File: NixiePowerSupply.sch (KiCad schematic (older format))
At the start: 1 part

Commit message: Preliminary schematic capture
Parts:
- added C1: 100uF, 35V, symbol CP
- added C2, C3: 100n, symbol C
- added C4: 4u7,250V, symbol CP
- added C5: 10uF,25V, symbol CP
- added D1: ES2F, symbol D
- added J?: BARREL_JACK, symbol BARREL_JACK
- added L1: 100uH, symbol L
- added R1: 10K, symbol R
- added R2: 1M5, symbol R
- added R?: RTRIM, symbol RTRIM
- added Rsense: 50m, symbol R
- added T1: IRF644, symbol IRF644
- gave numbers to parts that had none: 1
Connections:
- net labels added: GND, VCC
- wire segments 0 -> 38

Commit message: Add output capcacitor
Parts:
- added C6: 100nF, 250V, symbol C
- gave numbers to parts that had none: 1
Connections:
- wire segments 38 -> 42
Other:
- moved on the sheet: C4, D1, R1, R2, Rsense, T1
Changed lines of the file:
@@
 L IRF644 T1
 U 1 1 58D729C3
-P 6800 3400
-F 0 "T1" H 7000 3475 50  0000 L CNN
-F 1 "IRF644" H 7000 3400 50  0000 L CNN
-F 2 "" H 7000 3300 50  0001 L CIN
-F 3 "" H 6800 3400 50  0001 L CNN
-	1    6800 3400
+P 6600 3400
+F 0 "T1" H 6800 3475 50  0000 L CNN
+F 1 "IRF644" H 6800 3400 50  0000 L CNN
+F 2 "" H 6800 3300 50  0001 L CIN
+F 3 "" H 6600 3400 50  0001 L CNN
+	1    6600 3400
 	1    0    0    -1
 $EndComp
@@
 Connection ~ 4650 2600
 Wire Wire Line
-	6000 2600 6900 2600
-Wire Wire Line
-	6900 2600 6900 3200
-Wire Wire Line
-	6250 3450 6600 3450
+	6700 2600 6700 3200
 $Comp
 L CP C5
@@
 	5750 4300 5750 4000
 Wire Wire Line
-	3900 4300 8100 4300
+	8300 4300 3900 4300
 $Comp
 L GND #PWR?
@@
 L R Rsense
 U 1 1 58D73575
-P 6900 4050
-F 0 "Rsense" V 6980 4050 50  0000 C CNN
-F 1 "50m" V 6900 4050 50  0000 C CNN
-F 2 "" V 6830 4050 50  0001 C CNN
-F 3 "" H 6900 4050 50  0001 C CNN
-	1    6900 4050
-	1    0    0    -1
-$EndComp
-Wire Wire Line
-	6900 4300 6900 4200
+P 6700 4050
+F 0 "Rsense" V 6780 4050 50  0000 C CNN
+F 1 "50m" V 6700 4050 50  0000 C CNN
+F 2 "" V 6630 4050 50  0001 C CNN
+F 3 "" H 6700 4050 50  0001 C CNN
+	1    6700 4050
+	1    0    0    -1
+$EndComp
+Wire Wire Line
+	6700 4300 6700 4200
 Connection ~ 5750 4300
 Wire Wire Line
-	6900 3600 6900 3900
-Wire Wire Line
-	6750 3600 6750 3650
-Wire Wire Line
-	6750 3650 6900 3650
-Connection ~ 6900 3650
-Wire Wire Line
-	6750 3600 6250 3600
+	6700 3600 6700 3900
+Wire Wire Line
+	6550 3600 6550 3650
+Wire Wire Line
+	6550 3650 6700 3650
+Connection ~ 6700 3650
 $Comp
 L D D1
 U 1 1 58D73EA6
-P 7250 3050
-F 0 "D1" H 7250 3150 50  0000 C CNN
-F 1 "ES2F" H 7250 2950 50  0000 C CNN
-F 2 "" H 7250 3050 50  0001 C CNN
-F 3 "" H 7250 3050 50  0001 C CNN
-	1    7250 3050
+P 7050 3050
+F 0 "D1" H 7050 3150 50  0000 C CNN
+F 1 "ES2F" H 7050 2950 50  0000 C CNN
+F 2 "" H 7050 3050 50  0001 C CNN
+F 3 "" H 7050 3050 50  0001 C CNN
+	1    7050 3050
 	-1   0    0    1
 $EndComp
@@
 L CP C4
 U 1 1 58D74125
-P 7650 3400
-F 0 "C4" H 7675 3500 50  0000 L CNN
-F 1 "4u7,250V" H 7250 3300 50  0000 L CNN
-F 2 "" H 7688 3250 50  0001 C CNN
-F 3 "" H 7650 3400 50  0001 C CNN
-	1    7650 3400
-	1    0    0    -1
-$EndComp
-Wire Wire Line
-	7100 3050 6900 3050
-Connection ~ 6900 3050
-Wire Wire Line
-	7400 3050 8100 3050
-Wire Wire Line
-	7650 3050 7650 3250
-Wire Wire Line
-	7650 4300 7650 3550
-Connection ~ 6900 4300
+P 7350 3500
+F 0 "C4" H 7375 3600 50  0000 L CNN
+F 1 "4u7,250V" H 6950 3400 50  0000 L CNN
+F 2 "" H 7388 3350 50  0001 C CNN
+F 3 "" H 7350 3500 50  0001 C CNN
+	1    7350 3500
+	1    0    0    -1
+$EndComp
+Wire Wire Line
+	6900 3050 6700 3050
+Connection ~ 6700 3050
+Wire Wire Line
+	7200 3050 8300 3050
+Wire Wire Line
+	7350 3050 7350 3350
+Wire Wire Line
+	7350 4300 7350 3650
+Connection ~ 6700 4300
 $Comp
 L R R2
 U 1 1 58D74231
-P 8100 3250
-F 0 "R2" V 8180 3250 50  0000 C CNN
-F 1 "1M5" V 8100 3250 50  0000 C CNN
-F 2 "" V 8030 3250 50  0001 C CNN
-F 3 "" H 8100 3250 50  0001 C CNN
-	1    8100 3250
+P 7900 3250
+F 0 "R2" V 7980 3250 50  0000 C CNN
+F 1 "1M5" V 7900 3250 50  0000 C CNN
+F 2 "" V 7830 3250 50  0001 C CNN
+F 3 "" H 7900 3250 50  0001 C CNN
+	1    7900 3250
 	1    0    0    -1
 $EndComp
@@
 L R R1
 U 1 1 58D74274
-P 8100 4100
-F 0 "R1" V 8180 4100 50  0000 C CNN
-F 1 "10K" V 8100 4100 50  0000 C CNN
-F 2 "" V 8030 4100 50  0001 C CNN
-F 3 "" H 8100 4100 50  0001 C CNN
-	1    8100 4100
-	1    0    0    -1
-$EndComp
-Wire Wire Line
-	8100 3900 8100 3950
-$Comp
-L RTRIM R?
+P 7900 4100
+F 0 "R1" V 7980 4100 50  0000 C CNN
+F 1 "10K" V 7900 4100 50  0000 C CNN
+F 2 "" V 7830 4100 50  0001 C CNN
+F 3 "" H 7900 4100 50  0001 C CNN
+	1    7900 4100
+	1    0    0    -1
+$EndComp
+Wire Wire Line
+	7900 3900 7900 3950
+$Comp
+L RTRIM VR1
 U 1 1 58D74396
-P 8100 3750
-F 0 "R?" V 8200 3650 50  0000 L CNN
-F 1 "RTRIM" V 8000 3725 50  0000 L CNN
-F 2 "" V 8030 3750 50  0001 C CNN
-F 3 "" H 8100 3750 50  0001 C CNN
-	1    8100 3750
-	1    0    0    -1
-$EndComp
-Wire Wire Line
-	8100 3050 8100 3100
-Connection ~ 7650 3050
-Wire Wire Line
-	8100 3400 8100 3600
-Wire Wire Line
-	8100 4300 8100 4250
-Connection ~ 7650 4300
-Wire Wire Line
-	6250 3750 7900 3750
-Wire Wire Line
-	7900 3750 7900 3500
-Wire Wire Line
-	7900 3500 8100 3500
-Connection ~ 8100 3500
+P 7900 3750
+F 0 "VR1" V 8000 3650 50  0000 L CNN
+F 1 "RTRIM" V 7800 3725 50  0000 L CNN
+F 2 "" V 7830 3750 50  0001 C CNN
+F 3 "" H 7900 3750 50  0001 C CNN
+	1    7900 3750
+	1    0    0    -1
+$EndComp
+Wire Wire Line
+	7900 3050 7900 3100
+Connection ~ 7350 3050
+Wire Wire Line
+	7900 3400 7900 3600
+Wire Wire Line
+	7900 4300 7900 4250
+Connection ~ 7350 4300
+Wire Wire Line
+	7700 3750 7700 3500
+Wire Wire Line
+	7700 3500 7900 3500
+Connection ~ 7900 3500
+$Comp
+L C C6
+U 1 1 58D7E2B2
+P 8300 3650
+F 0 "C6" H 8325 3750 50  0000 L CNN
+F 1 "100nF, 250V" H 8325 3550 50  0000 L CNN
+F 2 "" H 8338 3500 50  0000 C CNN
+F 3 "" H 8300 3650 50  0000 C CNN
+	1    8300 3650
+	1    0    0    -1
+$EndComp
+Wire Wire Line
+	6000 2600 6700 2600
+Wire Wire Line
+	6250 3450 6400 3450
+Wire Wire Line
+	6250 3600 6550 3600
+Wire Wire Line
+	6250 3750 7700 3750
+Wire Wire Line
+	8300 3050 8300 3500
+Connection ~ 7900 3050
+Wire Wire Line
+	8300 3800 8300 4300
+Connection ~ 7900 4300
+Wire Wire Line
+	8300 3300 8500 3300
+Connection ~ 8300 3300
+Wire Wire Line
+	8300 4050 8500 4050
+Connection ~ 8300 4050
 $EndSCHEMATC

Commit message: Assigned some footprints.
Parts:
- C1, C5: footprint (none) -> Capacitors_Tantalum_SMD:CP_Tantalum_Case-X_EIA-7343-43_Hand
- C2, C3: footprint (none) -> Capacitors_SMD:C_0805_HandSoldering
- R1: footprint (none) -> Resistors_SMD:R_0805_HandSoldering
- R2: footprint (none) -> Resistors_SMD:R_2512_HandSoldering
- Rsense1: renamed from Rsense; footprint (none) -> Resistors_SMD:R_2010_HandSoldering
- T1: footprint (none) -> TO_SOT_Packages_THT:TO-220_Vertical
- U1: footprint (none) -> Housings_SOIC:SOIC-8_3.9x4.9mm_Pitch1.27mm
- gave numbers to parts that had none: 1
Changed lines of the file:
@@
 F 0 "U1" H 5850 2850 60  0000 C CNN
 F 1 "MAX1771" H 6000 3400 60  0000 C CNN
-F 2 "" H 5750 3350 60  0001 C CNN
+F 2 "Housings_SOIC:SOIC-8_3.9x4.9mm_Pitch1.27mm" H 5750 3350 60  0001 C CNN
 F 3 "" H 5750 3350 60  0001 C CNN
 	1    5750 3350
@@
 F 0 "C1" H 4675 2850 50  0000 L CNN
 F 1 "100uF, 35V" H 4675 2650 50  0000 L CNN
-F 2 "" H 4688 2600 50  0001 C CNN
+F 2 "Capacitors_Tantalum_SMD:CP_Tantalum_Case-X_EIA-7343-43_Hand" H 4688 2600 50  0001 C CNN
 F 3 "" H 4650 2750 50  0001 C CNN
 	1    4650 2750
@@
 F 0 "T1" H 6800 3475 50  0000 L CNN
 F 1 "IRF644" H 6800 3400 50  0000 L CNN
-F 2 "" H 6800 3300 50  0001 L CIN
+F 2 "TO_SOT_Packages_THT:TO-220_Vertical" H 6800 3300 50  0001 L CIN
 F 3 "" H 6600 3400 50  0001 L CNN
 	1    6600 3400
@@
 $EndComp
 $Comp
-L GND #PWR?
+L GND #PWR01
 U 1 1 58D72A4A
 P 4650 2950
-F 0 "#PWR?" H 4650 2700 50  0001 C CNN
+F 0 "#PWR01" H 4650 2700 50  0001 C CNN
 F 1 "GND" H 4650 2800 50  0000 C CNN
 F 2 "" H 4650 2950 50  0001 C CNN
@@
 F 0 "C5" H 4325 3950 50  0000 L CNN
 F 1 "10uF,25V" H 3950 3750 50  0000 L CNN
-F 2 "" H 4338 3700 50  0001 C CNN
+F 2 "Capacitors_Tantalum_SMD:CP_Tantalum_Case-X_EIA-7343-43_Hand" H 4338 3700 50  0001 C CNN
 F 3 "" H 4300 3850 50  0001 C CNN
 	1    4300 3850
@@
 	4650 2900 4650 2950
 $Comp
-L VCC #PWR?
+L VCC #PWR02
 U 1 1 58D72D8A
 P 4100 2550
-F 0 "#PWR?" H 4100 2400 50  0001 C CNN
+F 0 "#PWR02" H 4100 2400 50  0001 C CNN
 F 1 "VCC" H 4100 2700 50  0000 C CNN
 F 2 "" H 4100 2550 50  0001 C CNN
@@
 F 0 "C2" H 4675 3950 50  0000 L CNN
 F 1 "100n" H 4450 3750 50  0000 L CNN
-F 2 "" H 4688 3700 50  0001 C CNN
+F 2 "Capacitors_SMD:C_0805_HandSoldering" H 4688 3700 50  0001 C CNN
 F 3 "" H 4650 3850 50  0001 C CNN
 	1    4650 3850
@@
 F 0 "C3" H 4975 3950 50  0000 L CNN
 F 1 "100n" H 4750 3750 50  0000 L CNN
-F 2 "" H 4988 3700 50  0001 C CNN
+F 2 "Capacitors_SMD:C_0805_HandSoldering" H 4988 3700 50  0001 C CNN
 F 3 "" H 4950 3850 50  0001 C CNN
 	1    4950 3850
@@
 	8300 4300 3900 4300
 $Comp
-L GND #PWR?
+L GND #PWR03
 U 1 1 58D73109
 P 5400 4300
-F 0 "#PWR?" H 5400 4050 50  0001 C CNN
+F 0 "#PWR03" H 5400 4050 50  0001 C CNN
 F 1 "GND" H 5400 4150 50  0000 C CNN
 F 2 "" H 5400 4300 50  0001 C CNN
@@
 $EndComp
 $Comp
-L BARREL_JACK J?
+L BARREL_JACK J1
 U 1 1 58D73132
 P 3500 3900
-F 0 "J?" H 3500 4095 50  0000 C CNN
+F 0 "J1" H 3500 4095 50  0000 C CNN
 F 1 "BARREL_JACK" H 3500 3745 50  0000 C CNN
 F 2 "" H 3500 3900 50  0001 C CNN
@@
 Connection ~ 5150 4300
 $Comp
-L R Rsense
+L R Rsense1
 U 1 1 58D73575
 P 6700 4050
-F 0 "Rsense" V 6780 4050 50  0000 C CNN
+F 0 "Rsense1" V 6780 4050 50  0000 C CNN
 F 1 "50m" V 6700 4050 50  0000 C CNN
-F 2 "" V 6630 4050 50  0001 C CNN
+F 2 "Resistors_SMD:R_2010_HandSoldering" V 6630 4050 50  0001 C CNN
 F 3 "" H 6700 4050 50  0001 C CNN
 	1    6700 4050
@@
 F 0 "R2" V 7980 3250 50  0000 C CNN
 F 1 "1M5" V 7900 3250 50  0000 C CNN
-F 2 "" V 7830 3250 50  0001 C CNN
+F 2 "Resistors_SMD:R_2512_HandSoldering" V 7830 3250 50  0001 C CNN
 F 3 "" H 7900 3250 50  0001 C CNN
 	1    7900 3250
@@
 F 0 "R1" V 7980 4100 50  0000 C CNN
 F 1 "10K" V 7900 4100 50  0000 C CNN
-F 2 "" V 7830 4100 50  0001 C CNN
+F 2 "Resistors_SMD:R_0805_HandSoldering" V 7830 4100 50  0001 C CNN
 F 3 "" H 7900 4100 50  0001 C CNN
 	1    7900 4100
@@
 F 0 "C6" H 8325 3750 50  0000 L CNN
 F 1 "100nF, 250V" H 8325 3550 50  0000 L CNN
-F 2 "" H 8338 3500 50  0000 C CNN
+F 2 "" H 8338 3500 50  0001 C CNN
 F 3 "" H 8300 3650 50  0000 C CNN
 	1    8300 3650

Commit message: Add project footprint libary; start layout
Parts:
- C4: value 4u7,250V -> 10uF,250V
- D1: footprint (none) -> nixie:ES2F
- J1: footprint (none) -> Connectors:BARREL_JACK
- L1: footprint (none) -> nixie:L-B82479A1
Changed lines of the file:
@@
 F 0 "L1" V 5800 2600 50  0000 C CNN
 F 1 "100uH" V 5925 2600 50  0000 C CNN
-F 2 "" H 5850 2600 50  0001 C CNN
+F 2 "nixie:L-B82479A1" H 5850 2600 50  0001 C CNN
 F 3 "" H 5850 2600 50  0001 C CNN
 	1    5850 2600
@@
 F 0 "J1" H 3500 4095 50  0000 C CNN
 F 1 "BARREL_JACK" H 3500 3745 50  0000 C CNN
-F 2 "" H 3500 3900 50  0001 C CNN
+F 2 "Connectors:BARREL_JACK" H 3500 3900 50  0001 C CNN
 F 3 "" H 3500 3900 50  0001 C CNN
 	1    3500 3900
@@
 $EndComp
 Wire Wire Line
-	3800 3800 3900 3800
-Wire Wire Line
-	3900 3800 3900 4300
-Wire Wire Line
-	3850 4000 3800 4000
-Wire Wire Line
-	3850 2600 3850 4000
+	3850 2600 3850 3800
 Connection ~ 3850 3200
 Connection ~ 4100 2600
@@
 F 0 "D1" H 7050 3150 50  0000 C CNN
 F 1 "ES2F" H 7050 2950 50  0000 C CNN
-F 2 "" H 7050 3050 50  0001 C CNN
+F 2 "nixie:ES2F" H 7050 3050 50  0001 C CNN
 F 3 "" H 7050 3050 50  0001 C CNN
 	1    7050 3050
@@
 P 7350 3500
 F 0 "C4" H 7375 3600 50  0000 L CNN
-F 1 "4u7,250V" H 6950 3400 50  0000 L CNN
+F 1 "10uF,250V" H 6950 3400 50  0000 L CNN
 F 2 "" H 7388 3350 50  0001 C CNN
 F 3 "" H 7350 3500 50  0001 C CNN
@@
 	8300 4050 8500 4050
 Connection ~ 8300 4050
+Wire Wire Line
+	3850 3800 3800 3800
+Wire Wire Line
+	3900 4300 3900 4000
+Wire Wire Line
+	3900 4000 3800 4000
 $EndSCHEMATC

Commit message: Added cap and trimpot footprints
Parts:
- removed VR1: RTRIM, symbol RTRIM
- added VR1: 5K, nixie:Trimpot_Bourns_3214W, symbol POT_TRIM
- C4: footprint (none) -> Capacitors_SMD:CP_Elec_10x10
- C6: footprint (none) -> nixie:Panasonic_ECWU_Size_B
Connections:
- wire segments 42 -> 45
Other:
- note added: "Optional"
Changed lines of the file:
@@
 F 0 "C4" H 7375 3600 50  0000 L CNN
 F 1 "10uF,250V" H 6950 3400 50  0000 L CNN
-F 2 "" H 7388 3350 50  0001 C CNN
-F 3 "" H 7350 3500 50  0001 C CNN
+F 2 "Capacitors_SMD:CP_Elec_10x10" H 7388 3350 50  0001 C CNN
+F 3 "http://www.mouser.com/ds/2/315/ABA0000C1202-947653.pdf" H 7350 3500 50  0001 C CNN
 	1    7350 3500
 	1    0    0    -1
@@
 U 1 1 58D74231
 P 7900 3250
-F 0 "R2" V 7980 3250 50  0000 C CNN
+F 0 "R2" H 8000 3250 50  0000 C CNN
 F 1 "1M5" V 7900 3250 50  0000 C CNN
 F 2 "Resistors_SMD:R_2512_HandSoldering" V 7830 3250 50  0001 C CNN
@@
 U 1 1 58D74274
 P 7900 4100
-F 0 "R1" V 7980 4100 50  0000 C CNN
+F 0 "R1" H 8000 4100 50  0000 C CNN
 F 1 "10K" V 7900 4100 50  0000 C CNN
 F 2 "Resistors_SMD:R_0805_HandSoldering" V 7830 4100 50  0001 C CNN
@@
 $EndComp
 Wire Wire Line
-	7900 3900 7900 3950
-$Comp
-L RTRIM VR1
-U 1 1 58D74396
-P 7900 3750
-F 0 "VR1" V 8000 3650 50  0000 L CNN
-F 1 "RTRIM" V 7800 3725 50  0000 L CNN
-F 2 "" V 7830 3750 50  0001 C CNN
-F 3 "" H 7900 3750 50  0001 C CNN
-	1    7900 3750
-	1    0    0    -1
-$EndComp
+	7900 3850 7900 3950
 Wire Wire Line
 	7900 3050 7900 3100
 Connection ~ 7350 3050
 Wire Wire Line
-	7900 3400 7900 3600
+	7900 3400 7900 3550
 Wire Wire Line
 	7900 4300 7900 4250
@@
 F 0 "C6" H 8325 3750 50  0000 L CNN
 F 1 "100nF, 250V" H 8325 3550 50  0000 L CNN
-F 2 "" H 8338 3500 50  0001 C CNN
+F 2 "nixie:Panasonic_ECWU_Size_B" H 8338 3500 50  0001 C CNN
 F 3 "" H 8300 3650 50  0000 C CNN
 	1    8300 3650
@@
 Wire Wire Line
 	3900 4000 3800 4000
+$Comp
+L POT_TRIM VR1
+U 1 1 58DB1DC4
+P 7900 3700
+F 0 "VR1" H 8050 3800 50  0000 C CNN
+F 1 "5K" V 7900 3700 50  0000 C CNN
+F 2 "nixie:Trimpot_Bourns_3214W" H 7900 3700 50  0001 C CNN
+F 3 "" H 7900 3700 50  0001 C CNN
+	1    7900 3700
+	1    0    0    -1
+$EndComp
+Wire Wire Line
+	7900 3900 8100 3900
+Wire Wire Line
+	8100 3900 8100 3700
+Wire Wire Line
+	8100 3700 8050 3700
+Connection ~ 7900 3900
+Text Notes 8400 3900 0    60   ~ 0
+Optional
 $EndSCHEMATC

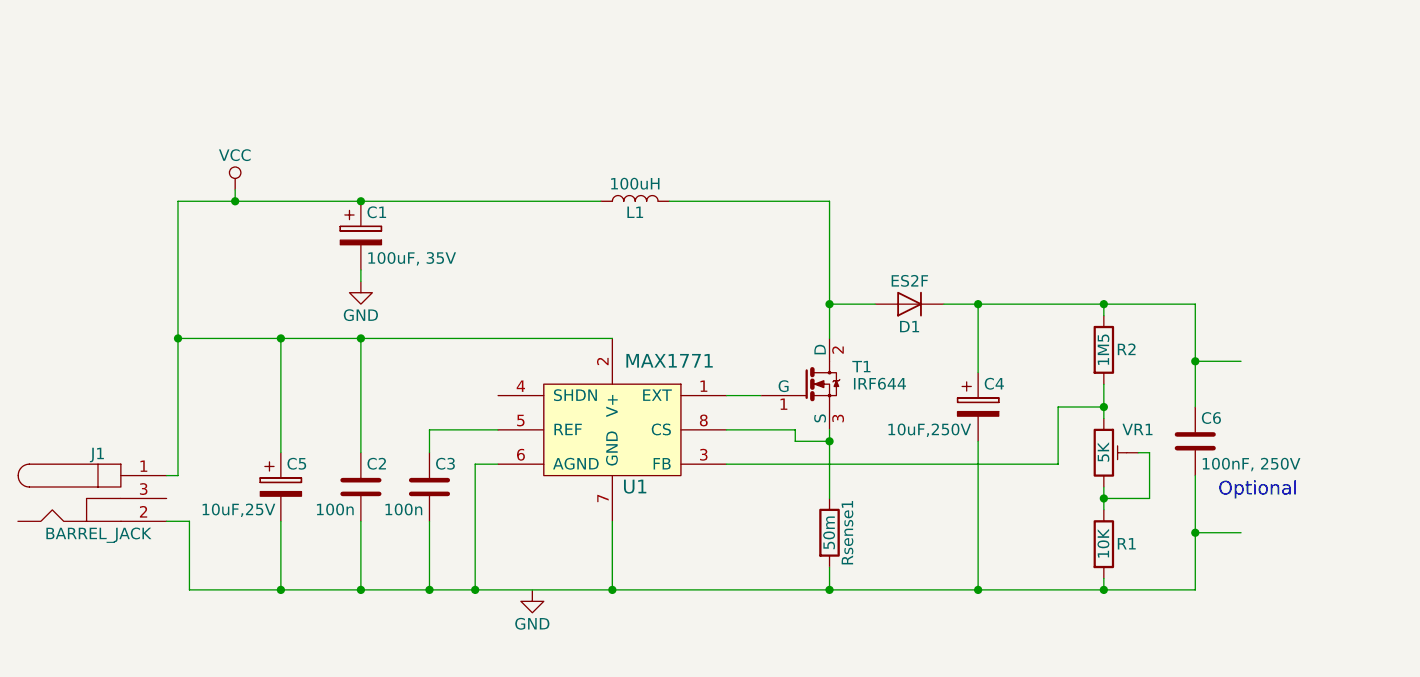
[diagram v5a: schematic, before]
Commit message: Add headers
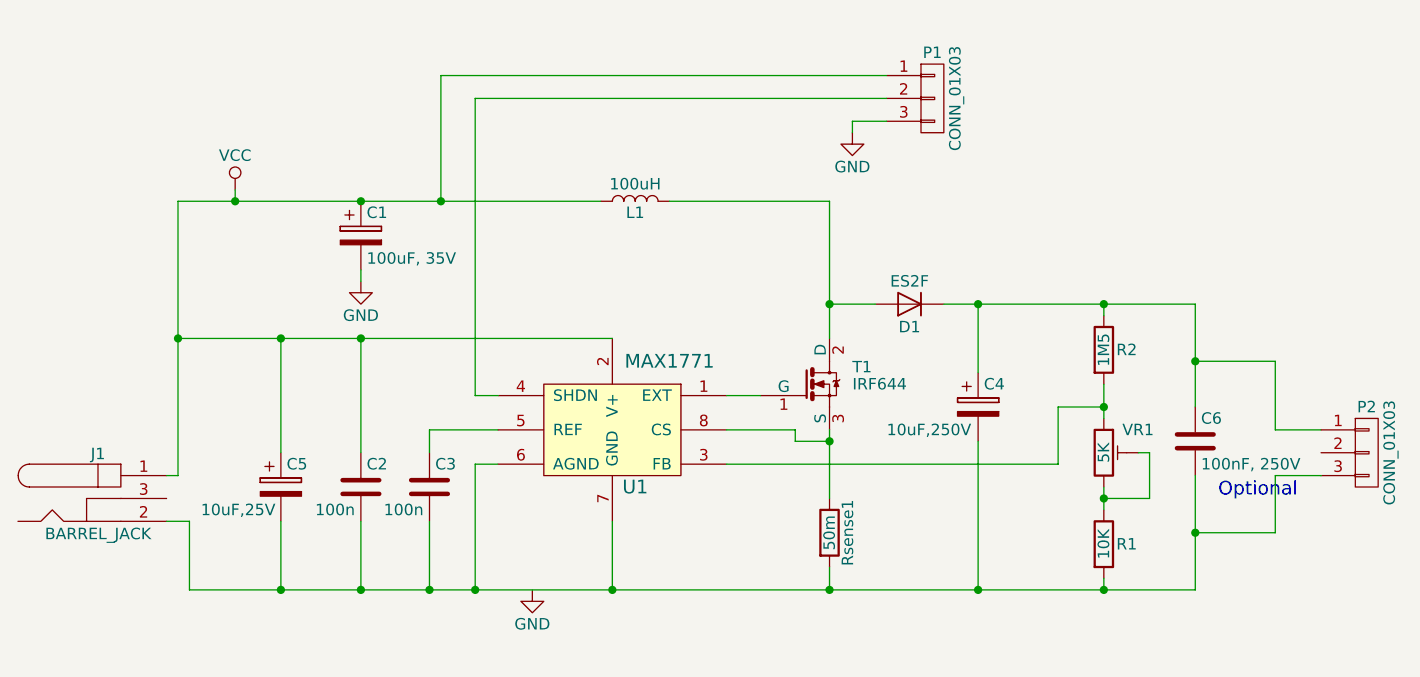
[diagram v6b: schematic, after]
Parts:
- added P1, P2: CONN_01X03, Pin_Headers:Pin_Header_Straight_1x03_Pitch2.54mm, symbol CONN_01X03
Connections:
- wire segments 45 -> 56
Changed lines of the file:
@@
 Connection ~ 7900 4300
 Wire Wire Line
-	8300 3300 8500 3300
+	8300 3300 8650 3300
 Connection ~ 8300 3300
 Wire Wire Line
-	8300 4050 8500 4050
+	8300 4050 8650 4050
 Connection ~ 8300 4050
 Wire Wire Line
@@
 Text Notes 8400 3900 0    60   ~ 0
 Optional
+$Comp
+L CONN_01X03 P2
+U 1 1 58DB3C7B
+P 9050 3700
+F 0 "P2" H 9050 3900 50  0000 C CNN
+F 1 "CONN_01X03" V 9150 3700 50  0000 C CNN
+F 2 "Pin_Headers:Pin_Header_Straight_1x03_Pitch2.54mm" H 9050 3700 50  0001 C CNN
+F 3 "" H 9050 3700 50  0000 C CNN
+	1    9050 3700
+	1    0    0    -1
+$EndComp
+Wire Wire Line
+	8650 3300 8650 3600
+Wire Wire Line
+	8650 3600 8850 3600
+Wire Wire Line
+	8650 4050 8650 3800
+Wire Wire Line
+	8650 3800 8850 3800
+$Comp
+L CONN_01X03 P1
+U 1 1 58DB3DD2
+P 7150 2150
+F 0 "P1" H 7150 2350 50  0000 C CNN
+F 1 "CONN_01X03" V 7250 2150 50  0000 C CNN
+F 2 "Pin_Headers:Pin_Header_Straight_1x03_Pitch2.54mm" H 7150 2150 50  0001 C CNN
+F 3 "" H 7150 2150 50  0000 C CNN
+	1    7150 2150
+	1    0    0    -1
+$EndComp
+Wire Wire Line
+	5000 2600 5000 2050
+Wire Wire Line
+	5000 2050 6950 2050
+Connection ~ 5000 2600
+Wire Wire Line
+	5250 3450 5150 3450
+Wire Wire Line
+	5150 3450 5150 2150
+Wire Wire Line
+	5150 2150 6950 2150
+$Comp
+L GND #PWR04
+U 1 1 58DB402E
+P 6800 2300
+F 0 "#PWR04" H 6800 2050 50  0001 C CNN
+F 1 "GND" H 6800 2150 50  0000 C CNN
+F 2 "" H 6800 2300 50  0000 C CNN
+F 3 "" H 6800 2300 50  0000 C CNN
+	1    6800 2300
+	1    0    0    -1
+$EndComp
+Wire Wire Line
+	6800 2300 6800 2250
+Wire Wire Line
+	6800 2250 6950 2250
 $EndSCHEMATC
